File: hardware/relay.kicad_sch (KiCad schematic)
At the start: 5 parts, among them K1 SRD-05VDC-SL-C, Q1 BC847

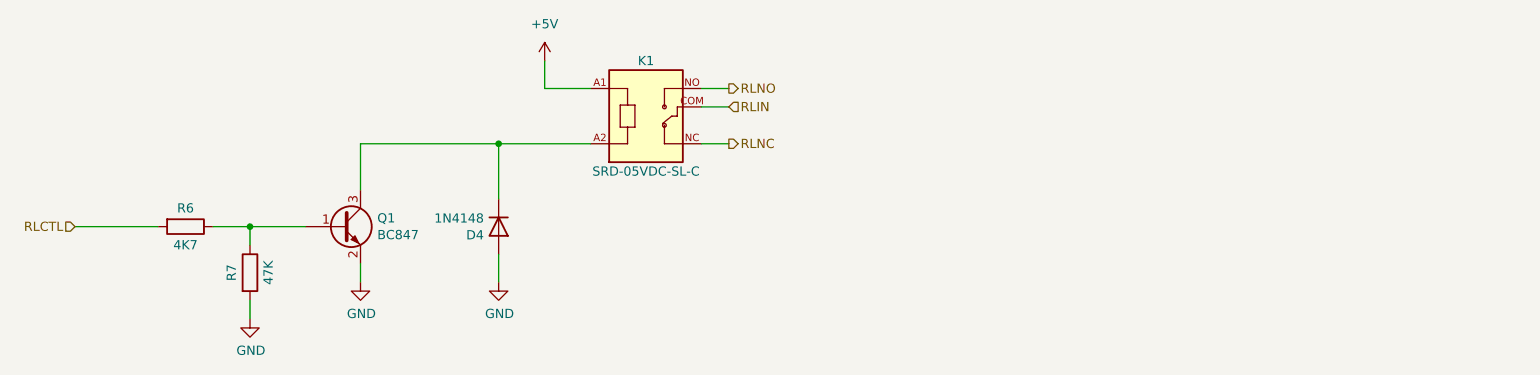
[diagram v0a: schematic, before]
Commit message: MCU BOOT0 mistake fixed
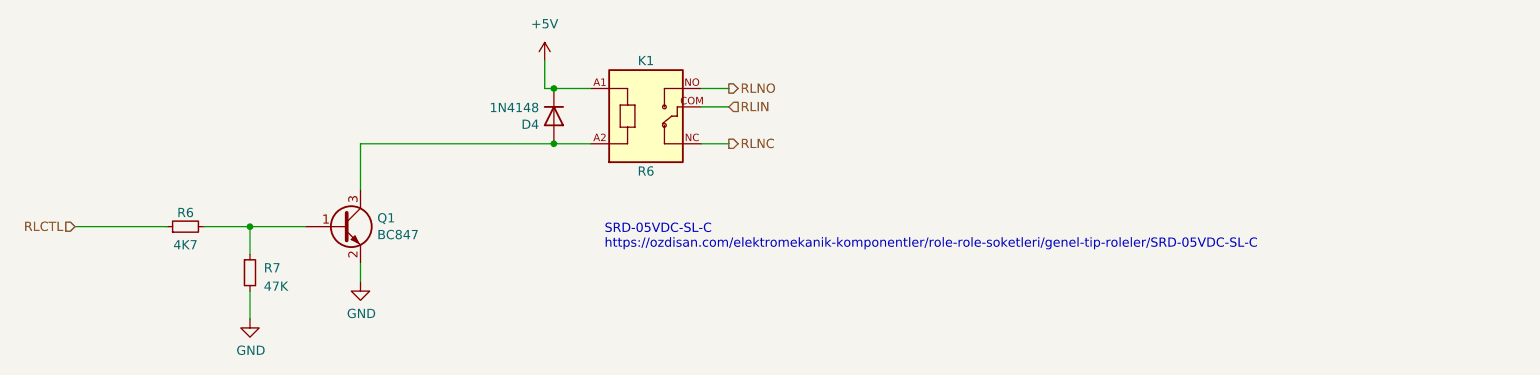
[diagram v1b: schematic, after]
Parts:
- removed R6: 4K7, Resistor_SMD:R_0603_1608Metric, symbol Device:R
- removed R7: 47K, Resistor_SMD:R_0603_1608Metric, symbol Device:R
- added R6: 4K7, Resistor_SMD:R_0603_1608Metric, symbol Device:R_Small
- added R7: 47K, Resistor_SMD:R_0603_1608Metric, symbol Device:R_Small
- D4: Digikey 1086-15206-ND -> (none); DigikeyPN (none) -> 1086-15206-ND
- K1: value SRD-05VDC-SL-C -> R6; now left out of the parts list
- Q1: Digikey 3757-BC847C_R1_00001DKR-ND -> (none); DigikeyPN (none) -> 3757-BC847C_R1_00001DKR-ND
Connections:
- net +5V: now also D4.1 (K)
- net GND: now also R7.2; no longer D4.2 (A)
- net RLCTL: now also R6.1
- net at Q1.1 (B): now also R6.2, R7.1
- net at K1.A2, Q1.3 (C): now also D4.2 (A); no longer D4.1 (K)
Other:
- note added: "SRD-05VDC-SL-C https://ozdisan.com/elektromekanik-komponentler/role-role-soketleri/genel-tip-roleler/SRD-05VDC-SL-C"
- moved on the sheet: D4
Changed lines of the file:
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@@
   (junction (at 123.825 101.6) (diameter 0) (color 0 0 0 0)
   )
-  (junction (at 158.115 90.17) (diameter 0) (color 0 0 0 0)
-  )
-  (wire (pts (xy 158.115 90.17) (xy 170.815 90.17))
-    (stroke (width 0) (type default))
+  (junction (at 165.735 90.17) (diameter 0) (color 0 0 0 0)
+  )
+  (junction (at 165.735 82.55) (diameter 0) (color 0 0 0 0)
   )
   (wire (pts (xy 139.065 90.17) (xy 139.065 96.52))
@@
     (stroke (width 0) (type default))
   )
-  (wire (pts (xy 123.825 104.14) (xy 123.825 101.6))
+  (wire (pts (xy 123.825 101.6) (xy 123.825 105.41))
     (stroke (width 0) (type default))
   )
@@
     (stroke (width 0) (type default))
   )
+  (wire (pts (xy 165.735 90.17) (xy 170.815 90.17))
+    (stroke (width 0) (type default))
+  )
   (wire (pts (xy 164.465 78.74) (xy 164.465 82.55))
     (stroke (width 0) (type default))
@@
     (stroke (width 0) (type default))
   )
+  (wire (pts (xy 165.735 82.55) (xy 170.815 82.55))
+    (stroke (width 0) (type default))
+  )
   (wire (pts (xy 186.055 85.09) (xy 189.865 85.09))
     (stroke (width 0) (type default))
   )
-  (wire (pts (xy 158.115 90.17) (xy 158.115 97.79))
-    (stroke (width 0) (type default))
-  )
-  (wire (pts (xy 164.465 82.55) (xy 170.815 82.55))
-    (stroke (width 0) (type default))
-  )
-  (wire (pts (xy 118.745 101.6) (xy 123.825 101.6))
-    (stroke (width 0) (type default))
-  )
-  (wire (pts (xy 123.825 114.3) (xy 123.825 111.76))
+  (wire (pts (xy 164.465 82.55) (xy 165.735 82.55))
+    (stroke (width 0) (type default))
+  )
+  (wire (pts (xy 117.475 101.6) (xy 123.825 101.6))
     (stroke (width 0) (type default))
   )
@@
     (stroke (width 0) (type default))
   )
-  (wire (pts (xy 99.695 101.6) (xy 111.125 101.6))
-    (stroke (width 0) (type default))
-  )
-  (wire (pts (xy 139.065 90.17) (xy 158.115 90.17))
-    (stroke (width 0) (type default))
-  )
-  (wire (pts (xy 158.115 105.41) (xy 158.115 109.22))
-    (stroke (width 0) (type default))
+  (wire (pts (xy 99.695 101.6) (xy 112.395 101.6))
+    (stroke (width 0) (type default))
+  )
+  (wire (pts (xy 139.065 90.17) (xy 165.735 90.17))
+    (stroke (width 0) (type default))
+  )
+  (wire (pts (xy 123.825 110.49) (xy 123.825 114.3))
+    (stroke (width 0) (type default))
+  )
+  (text "SRD-05VDC-SL-C\nhttps://ozdisan.com/elektromekanik-komponentler/role-role-soketleri/genel-tip-roleler/SRD-05VDC-SL-C"
+    (at 172.72 104.775 0)
+    (effects (font (size 1.27 1.27)) (justify left bottom) (href "https://ozdisan.com/elektromekanik-komponentler/role-role-soketleri/genel-tip-roleler/SRD-05VDC-SL-C"))
   )
   (hierarchical_label "RLIN" (shape input) (at 189.865 85.09 0) (fields_autoplaced)
@@
     (effects (font (size 1.27 1.27)) (justify left))
   )
-  (symbol (lib_id "power:GND") (at 158.115 109.22 0) (unit 1)
-    (in_bom yes) (on_board yes) (dnp no)
-    (property "Reference" "#PWR028" (at 158.115 115.57 0)
-      (effects (font (size 1.27 1.27)) hide)
-    )
-    (property "Value" "GND" (at 158.242 113.6142 0)
-      (effects (font (size 1.27 1.27)))
-    )
-    (property "Footprint" "" (at 158.115 109.22 0)
-      (effects (font (size 1.27 1.27)) hide)
-    )
-    (property "Datasheet" "" (at 158.115 109.22 0)
-      (effects (font (size 1.27 1.27)) hide)
-    )
-    (pin "1")
-    (instances
-      (project "damlama"
-        (path "/03f54461-a23f-4bbd-ad19-ab4264ed7ebc/4a05dca8-55e2-47f0-9b7c-f520024a12fb"
-          (reference "#PWR028") (unit 1)
-        )
-      )
-      (project "damlama"
-        (path "/4173cfe1-9b8e-4ca0-b697-667c7ccea108/df29bdd5-d08b-4222-b4e8-0c9ddd22a013"
-          (reference "#PWR031") (unit 1)
-        )
-      )
-    )
-  )
-  (symbol (lib_id "Device:R") (at 114.935 101.6 270) (unit 1)
-    (in_bom yes) (on_board yes) (dnp no)
-    (property "Reference" "R6" (at 114.935 99.06 90)
-      (effects (font (size 1.27 1.27)))
-    )
-    (property "Value" "4K7" (at 114.935 104.14 90)
-      (effects (font (size 1.27 1.27)))
-    )
-    (property "Footprint" "Resistor_SMD:R_0603_1608Metric" (at 114.935 99.822 90)
-      (effects (font (size 1.27 1.27)) hide)
-    )
-    (property "Datasheet" "~" (at 114.935 101.6 0)
-      (effects (font (size 1.27 1.27)) hide)
-    )
-    (property "Digikey" "311-47.0KHRCT-ND" (at 114.935 101.6 90)
+  (symbol (lib_id "Device:R_Small") (at 123.825 107.95 0) (unit 1)
+    (in_bom yes) (on_board yes) (dnp no) (fields_autoplaced)
+    (property "Reference" "R7" (at 125.73 107.315 0)
+      (effects (font (size 1.27 1.27)) (justify left))
+    )
+    (property "Value" "47K" (at 125.73 109.855 0)
+      (effects (font (size 1.27 1.27)) (justify left))
+    )
+    (property "Footprint" "Resistor_SMD:R_0603_1608Metric" (at 123.825 107.95 0)
+      (effects (font (size 1.27 1.27)) hide)
+    )
+    (property "Datasheet" "~" (at 123.825 107.95 0)
+      (effects (font (size 1.27 1.27)) hide)
+    )
+    (property "DigikeyPN" "311-47.0KHRCT-ND" (at 123.825 107.95 0)
       (effects (font (size 1.27 1.27)) hide)
     )
@@
       (project "damlama"
         (path "/03f54461-a23f-4bbd-ad19-ab4264ed7ebc/4a05dca8-55e2-47f0-9b7c-f520024a12fb"
-          (reference "R6") (unit 1)
-        )
-      )
-      (project "damlama"
-        (path "/4173cfe1-9b8e-4ca0-b697-667c7ccea108/df29bdd5-d08b-4222-b4e8-0c9ddd22a013"
-          (reference "R5") (unit 1)
+          (reference "R7") (unit 1)
         )
       )
@@
       (effects (font (size 1.27 1.27)) (justify left) hide)
     )
-    (property "Digikey" "3757-BC847C_R1_00001DKR-ND" (at 136.525 101.6 0)
+    (property "DigikeyPN" "3757-BC847C_R1_00001DKR-ND" (at 136.525 101.6 0)
       (effects (font (size 1.27 1.27)) hide)
     )
@@
         (path "/4173cfe1-9b8e-4ca0-b697-667c7ccea108/df29bdd5-d08b-4222-b4e8-0c9ddd22a013"
           (reference "Q1") (unit 1)
+        )
+      )
+    )
+  )
+  (symbol (lib_id "Device:R_Small") (at 114.935 101.6 90) (unit 1)
+    (in_bom yes) (on_board yes) (dnp no)
+    (property "Reference" "R6" (at 114.935 99.695 90)
+      (effects (font (size 1.27 1.27)))
+    )
+    (property "Value" "4K7" (at 114.935 104.14 90)
+      (effects (font (size 1.27 1.27)))
+    )
+    (property "Footprint" "Resistor_SMD:R_0603_1608Metric" (at 114.935 101.6 0)
+      (effects (font (size 1.27 1.27)) hide)
+    )
+    (property "Datasheet" "~" (at 114.935 101.6 0)
+      (effects (font (size 1.27 1.27)) hide)
+    )
+    (property "DigikeyPN" "13-RC1206FR-134K7LDKR-ND" (at 114.935 101.6 90)
+      (effects (font (size 1.27 1.27)) hide)
+    )
+    (pin "1")
+    (pin "2")
+    (instances
+      (project "damlama"
+        (path "/03f54461-a23f-4bbd-ad19-ab4264ed7ebc/4a05dca8-55e2-47f0-9b7c-f520024a12fb"
+          (reference "R6") (unit 1)
         )
       )
@@
     )
   )
-  (symbol (lib_id "Diode:1N4148") (at 158.115 101.6 270) (unit 1)
-    (in_bom yes) (on_board yes) (dnp no)
-    (property "Reference" "D4" (at 156.083 102.7684 90)
+  (symbol (lib_id "Diode:1N4148") (at 165.735 86.36 270) (unit 1)
+    (in_bom yes) (on_board yes) (dnp no)
+    (property "Reference" "D4" (at 163.703 87.5284 90)
       (effects (font (size 1.27 1.27)) (justify right))
     )
-    (property "Value" "1N4148" (at 156.083 100.457 90)
+    (property "Value" "1N4148" (at 163.703 85.217 90)
       (effects (font (size 1.27 1.27)) (justify right))
     )
-    (property "Footprint" "Diode_SMD:D_MiniMELF" (at 153.67 101.6 0)
-      (effects (font (size 1.27 1.27)) hide)
-    )
-    (property "Datasheet" "https://assets.nexperia.com/documents/data-sheet/1N4148_1N4448.pdf" (at 158.115 101.6 0)
-      (effects (font (size 1.27 1.27)) hide)
-    )
-    (property "Digikey" "1086-15206-ND" (at 158.115 101.6 90)
+    (property "Footprint" "Diode_SMD:D_MiniMELF" (at 161.29 86.36 0)
+      (effects (font (size 1.27 1.27)) hide)
+    )
+    (property "Datasheet" "https://assets.nexperia.com/documents/data-sheet/1N4148_1N4448.pdf" (at 165.735 86.36 0)
+      (effects (font (size 1.27 1.27)) hide)
+    )
+    (property "DigikeyPN" "1086-15206-ND" (at 165.735 86.36 90)
       (effects (font (size 1.27 1.27)) hide)
     )
@@
   )
   (symbol (lib_id "Damlama:SRD-05VDC-SL-C") (at 178.435 85.09 0) (unit 1)
-    (in_bom yes) (on_board yes) (dnp no)
+    (in_bom no) (on_board yes) (dnp no)
     (property "Reference" "K1" (at 178.435 78.74 0)
       (effects (font (size 1.27 1.27)))
     )
-    (property "Value" "SRD-05VDC-SL-C" (at 178.435 93.98 0)
+    (property "Value" "R6" (at 178.435 93.98 0)
       (effects (font (size 1.27 1.27)))
     )
@@
         )
       )
-    )
-  )
-  (symbol (lib_id "Device:R") (at 123.825 107.95 0) (unit 1)
-    (in_bom yes) (on_board yes) (dnp no)
-    (property "Reference" "R7" (at 121.285 107.95 90)
-      (effects (font (size 1.27 1.27)))
-    )
-    (property "Value" "47K" (at 126.365 107.95 90)
-      (effects (font (size 1.27 1.27)))
-    )
-    (property "Footprint" "Resistor_SMD:R_0603_1608Metric" (at 122.047 107.95 90)
-      (effects (font (size 1.27 1.27)) hide)
-    )
-    (property "Datasheet" "~" (at 123.825 107.95 0)
-      (effects (font (size 1.27 1.27)) hide)
-    )
-    (property "Digikey" "311-47.0KHRCT-ND" (at 123.825 107.95 90)
-      (effects (font (size 1.27 1.27)) hide)
-    )
-    (pin "1")
-    (pin "2")
-    (instances
-      (project "damlama"
-        (path "/03f54461-a23f-4bbd-ad19-ab4264ed7ebc/4a05dca8-55e2-47f0-9b7c-f520024a12fb"
-          (reference "R7") (unit 1)
-        )
-      )
-      (project "damlama"
-        (path "/4173cfe1-9b8e-4ca0-b697-667c7ccea108/df29bdd5-d08b-4222-b4e8-0c9ddd22a013"
-          (reference "R6") (unit 1)
-        )
-      )
